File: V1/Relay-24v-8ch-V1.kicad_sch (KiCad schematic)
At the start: 49 parts, among them J1 Conn_01x09, J3 OUT1, J3 OUT2, J3 OUT3, J3 OUT4, J3 OUT5, J3 OUT6, J3 OUT7, J3 OUT8, K1 G5PZ-1A

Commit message: Change connector 3D model
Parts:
- J1: footprint Tales:TerminalBlock_Dorabo_DB141V-2.54-09P_1x09_P2.54mm_Vertical -> Tales:TerminalBlock_DG141V-2.54-9P_1x09_P2.54mm_Vertical
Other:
- title: (none) -> 8x 24V Relay Module

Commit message: Update to silkscreen and board image.
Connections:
- net +24V: now also J1.9 (Pin_9); no longer J1.1 (Pin_1)
- net at D14.1 (K), D15.2 (A), K1.4: now also J1.2 (Pin_2); no longer J1.8 (Pin_8)
- net at D14.1 (K), D15.2 (A), K1.4: now also J1.6 (Pin_6); no longer J1.4 (Pin_4)
- net at D14.1 (K), D15.2 (A), K1.4: now also J1.8 (Pin_8); no longer J1.2 (Pin_2)
- net at D14.1 (K), D15.2 (A), K1.4: now also J1.3 (Pin_3); no longer J1.7 (Pin_7)
- net at D14.1 (K), D15.2 (A), K1.4: now also J1.4 (Pin_4); no longer J1.6 (Pin_6)
- net at D14.1 (K), D15.2 (A), K1.4: now also J1.1 (Pin_1); no longer J1.9 (Pin_9)
- net at D14.1 (K), D15.2 (A), K1.4: now also J1.7 (Pin_7); no longer J1.3 (Pin_3)
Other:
- moved on the sheet: J1
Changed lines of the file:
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@@
     )
   )
-  (symbol (lib_id "Connector_Generic:Conn_01x09") (at 25.4 54.61 0) (mirror y) (unit 1)
-    (in_bom yes) (on_board yes) (dnp no) (fields_autoplaced)
-    (property "Reference" "J1" (at 25.4 39.37 0)
+  (symbol (lib_id "Connector_Generic:Conn_01x09") (at 25.4 54.61 180) (unit 1)
+    (in_bom yes) (on_board yes) (dnp no)
+    (property "Reference" "J1" (at 25.4 38.1 0)
       (effects (font (size 1.27 1.27)))
     )
-    (property "Value" "Conn_01x09" (at 25.4 41.91 0)
+    (property "Value" "Conn_01x09" (at 25.4 40.64 0)
       (effects (font (size 1.27 1.27)))
     )

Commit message: Adjustments for fabrication
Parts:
- D14: value BLUE/0603 -> GREEN/0603; LCSC Part # C72041 -> C72043; Mfr PN 19-217/BHC-ZL1M2RY/3T -> 19-217/GHC-YR1S2/3T; Vendor PN C72041 -> C72043
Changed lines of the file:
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@@
       (effects (font (size 1.27 1.27)) (justify left))
     )
-    (property "Value" "BLUE/0603" (at 68.58 153.67 90)
+    (property "Value" "GREEN/0603" (at 68.58 153.67 90)
       (effects (font (size 1.27 1.27)) (justify left))
     )
@@
       (effects (font (size 1.27 1.27)) hide)
     )
-    (property "Mfr PN" "19-217/BHC-ZL1M2RY/3T" (at 71.12 153.67 0)
+    (property "Mfr PN" "19-217/GHC-YR1S2/3T" (at 71.12 153.67 0)
       (effects (font (size 1.27 1.27)) hide)
     )
@@
       (effects (font (size 1.27 1.27)) hide)
     )
-    (property "Vendor PN" "C72041" (at 71.12 153.67 0)
-      (effects (font (size 1.27 1.27)) hide)
-    )
-    (property "LCSC Part #" "C72041" (at 68.58 156.21 90)
+    (property "Vendor PN" "C72043" (at 71.12 153.67 0)
+      (effects (font (size 1.27 1.27)) hide)
+    )
+    (property "LCSC Part #" "C72043" (at 68.58 156.21 90)
       (effects (font (size 1.27 1.27)) (justify left))
     )
@@
       (effects (font (size 1.27 1.27)) (justify left))
     )
-    (property "Value" "BLUE/0603" (at 171.45 78.74 90)
+    (property "Value" "GREEN/0603" (at 171.45 78.74 90)
       (effects (font (size 1.27 1.27)) (justify left))
     )
@@
       (effects (font (size 1.27 1.27)) hide)
     )
-    (property "Mfr PN" "19-217/BHC-ZL1M2RY/3T" (at 173.99 78.74 0)
+    (property "Mfr PN" "19-217/GHC-YR1S2/3T" (at 173.99 78.74 0)
       (effects (font (size 1.27 1.27)) hide)
     )
@@
       (effects (font (size 1.27 1.27)) hide)
     )
-    (property "Vendor PN" "C72041" (at 173.99 78.74 0)
-      (effects (font (size 1.27 1.27)) hide)
-    )
-    (property "LCSC Part #" "C72041" (at 171.45 81.28 90)
+    (property "Vendor PN" "C72043" (at 173.99 78.74 0)
+      (effects (font (size 1.27 1.27)) hide)
+    )
+    (property "LCSC Part #" "C72043" (at 171.45 81.28 90)
       (effects (font (size 1.27 1.27)) (justify left))
     )
@@
       (effects (font (size 1.27 1.27)) (justify left))
     )
-    (property "Value" "BLUE/0603" (at 68.58 116.84 90)
+    (property "Value" "GREEN/0603" (at 68.58 116.84 90)
       (effects (font (size 1.27 1.27)) (justify left))
     )
@@
       (effects (font (size 1.27 1.27)) hide)
     )
-    (property "Mfr PN" "19-217/BHC-ZL1M2RY/3T" (at 71.12 116.84 0)
+    (property "Mfr PN" "19-217/GHC-YR1S2/3T" (at 71.12 116.84 0)
       (effects (font (size 1.27 1.27)) hide)
     )
@@
       (effects (font (size 1.27 1.27)) hide)
     )
-    (property "Vendor PN" "C72041" (at 71.12 116.84 0)
-      (effects (font (size 1.27 1.27)) hide)
-    )
-    (property "LCSC Part #" "C72041" (at 68.58 119.38 90)
+    (property "Vendor PN" "C72043" (at 71.12 116.84 0)
+      (effects (font (size 1.27 1.27)) hide)
+    )
+    (property "LCSC Part #" "C72043" (at 68.58 119.38 90)
       (effects (font (size 1.27 1.27)) (justify left))
     )
@@
       (effects (font (size 1.27 1.27)) (justify left))
     )
-    (property "Value" "BLUE/0603" (at 68.58 78.74 90)
+    (property "Value" "GREEN/0603" (at 68.58 78.74 90)
       (effects (font (size 1.27 1.27)) (justify left))
     )
@@
       (effects (font (size 1.27 1.27)) hide)
     )
-    (property "Mfr PN" "19-217/BHC-ZL1M2RY/3T" (at 71.12 78.74 0)
+    (property "Mfr PN" "19-217/GHC-YR1S2/3T" (at 71.12 78.74 0)
       (effects (font (size 1.27 1.27)) hide)
     )
@@
       (effects (font (size 1.27 1.27)) hide)
     )
-    (property "Vendor PN" "C72041" (at 71.12 78.74 0)
-      (effects (font (size 1.27 1.27)) hide)
-    )
-    (property "LCSC Part #" "C72041" (at 68.58 81.28 90)
+    (property "Vendor PN" "C72043" (at 71.12 78.74 0)
+      (effects (font (size 1.27 1.27)) hide)
+    )
+    (property "LCSC Part #" "C72043" (at 68.58 81.28 90)
       (effects (font (size 1.27 1.27)) (justify left))
     )
@@
       (effects (font (size 1.27 1.27)) (justify left))
     )
-    (property "Value" "BLUE/0603" (at 171.45 153.67 90)
+    (property "Value" "GREEN/0603" (at 171.45 153.67 90)
       (effects (font (size 1.27 1.27)) (justify left))
     )
@@
       (effects (font (size 1.27 1.27)) hide)
     )
-    (property "Mfr PN" "19-217/BHC-ZL1M2RY/3T" (at 173.99 153.67 0)
+    (property "Mfr PN" "19-217/GHC-YR1S2/3T" (at 173.99 153.67 0)
       (effects (font (size 1.27 1.27)) hide)
     )
@@
       (effects (font (size 1.27 1.27)) hide)
     )
-    (property "Vendor PN" "C72041" (at 173.99 153.67 0)
-      (effects (font (size 1.27 1.27)) hide)
-    )
-    (property "LCSC Part #" "C72041" (at 171.45 156.21 90)
+    (property "Vendor PN" "C72043" (at 173.99 153.67 0)
+      (effects (font (size 1.27 1.27)) hide)
+    )
+    (property "LCSC Part #" "C72043" (at 171.45 156.21 90)
       (effects (font (size 1.27 1.27)) (justify left))
     )
@@
       (effects (font (size 1.27 1.27)) (justify left))
     )
-    (property "Value" "BLUE/0603" (at 68.58 40.64 90)
+    (property "Value" "GREEN/0603" (at 68.58 40.64 90)
       (effects (font (size 1.27 1.27)) (justify left))
     )
@@
       (effects (font (size 1.27 1.27)) hide)
     )
-    (property "Mfr PN" "19-217/BHC-ZL1M2RY/3T" (at 71.12 40.64 0)
+    (property "Mfr PN" "19-217/GHC-YR1S2/3T" (at 71.12 40.64 0)
       (effects (font (size 1.27 1.27)) hide)
     )
@@
       (effects (font (size 1.27 1.27)) hide)
     )
-    (property "Vendor PN" "C72041" (at 71.12 40.64 0)
-      (effects (font (size 1.27 1.27)) hide)
-    )
-    (property "LCSC Part #" "C72041" (at 68.58 43.18 90)
+    (property "Vendor PN" "C72043" (at 71.12 40.64 0)
+      (effects (font (size 1.27 1.27)) hide)
+    )
+    (property "LCSC Part #" "C72043" (at 68.58 43.18 90)
       (effects (font (size 1.27 1.27)) (justify left))
     )
@@
       (effects (font (size 1.27 1.27)) (justify left))
     )
-    (property "Value" "BLUE/0603" (at 171.45 116.84 90)
+    (property "Value" "GREEN/0603" (at 171.45 116.84 90)
       (effects (font (size 1.27 1.27)) (justify left))
     )
@@
       (effects (font (size 1.27 1.27)) hide)
     )
-    (property "Mfr PN" "19-217/BHC-ZL1M2RY/3T" (at 173.99 116.84 0)
+    (property "Mfr PN" "19-217/GHC-YR1S2/3T" (at 173.99 116.84 0)
       (effects (font (size 1.27 1.27)) hide)
     )
@@
       (effects (font (size 1.27 1.27)) hide)
     )
-    (property "Vendor PN" "C72041" (at 173.99 116.84 0)
-      (effects (font (size 1.27 1.27)) hide)
-    )
-    (property "LCSC Part #" "C72041" (at 171.45 119.38 90)
+    (property "Vendor PN" "C72043" (at 173.99 116.84 0)
+      (effects (font (size 1.27 1.27)) hide)
+    )
+    (property "LCSC Part #" "C72043" (at 171.45 119.38 90)
       (effects (font (size 1.27 1.27)) (justify left))
     )
@@
       (effects (font (size 1.27 1.27)) (justify left))
     )
-    (property "Value" "BLUE/0603" (at 171.45 40.64 90)
+    (property "Value" "GREEN/0603" (at 171.45 40.64 90)
       (effects (font (size 1.27 1.27)) (justify left))
     )
@@
       (effects (font (size 1.27 1.27)) hide)
     )
-    (property "Mfr PN" "19-217/BHC-ZL1M2RY/3T" (at 173.99 40.64 0)
+    (property "Mfr PN" "19-217/GHC-YR1S2/3T" (at 173.99 40.64 0)
       (effects (font (size 1.27 1.27)) hide)
     )
@@
       (effects (font (size 1.27 1.27)) hide)
     )
-    (property "Vendor PN" "C72041" (at 173.99 40.64 0)
-      (effects (font (size 1.27 1.27)) hide)
-    )
-    (property "LCSC Part #" "C72041" (at 171.45 43.18 90)
-      (effects (font (size 1.27 1.27)) (justify left))
-    )
+    (property "Vendor PN" "C72043" (at 173.99 40.64 0)
+      (effects (font (size 1.27 1.27)) hide)
+    )
+    (property "LCSC Part #" "C72043" (at 171.45 43.18 90)
+      (effects (font (size 1.27 1.27)) (justify left))
+    )

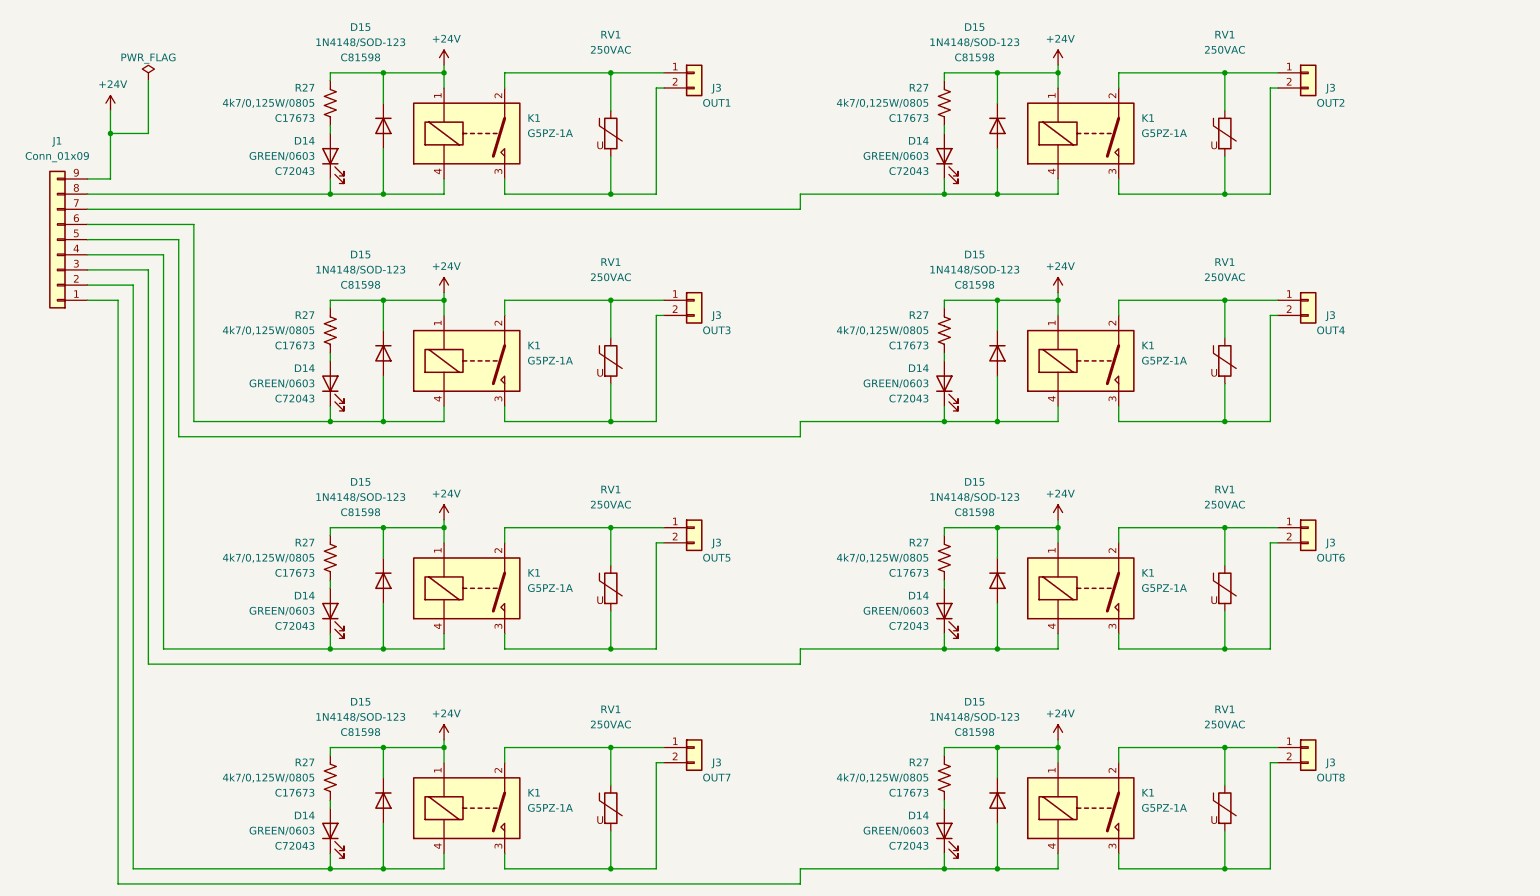
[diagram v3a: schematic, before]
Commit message: Varistor updated
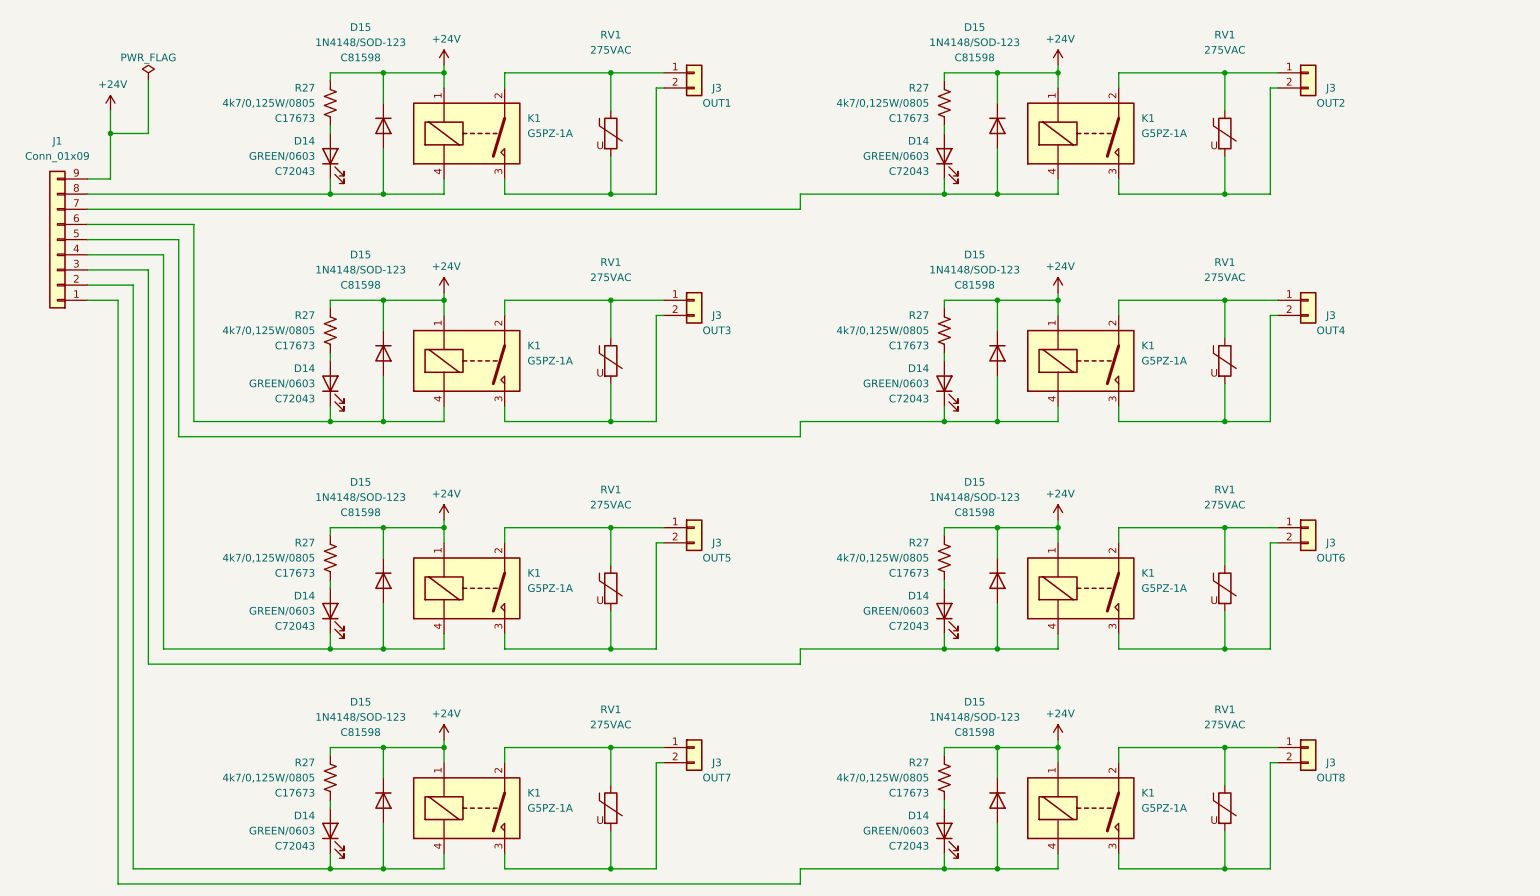
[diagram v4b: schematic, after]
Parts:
- RV1: value 250VAC -> 275VAC; Mfr PN 391KD10 -> 431KD10; Vendor PN 603-391KD10 -> 603-431KD10
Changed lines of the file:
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@@
       (effects (font (size 1.27 1.27)))
     )
-    (property "Value" "250VAC" (at 118.11 99.06 0)
+    (property "Value" "275VAC" (at 118.11 99.06 0)
       (effects (font (size 1.27 1.27)))
     )
@@
       (effects (font (size 1.27 1.27)) hide)
     )
-    (property "Mfr PN" "391KD10" (at 118.11 113.03 0)
+    (property "Mfr PN" "431KD10" (at 118.11 113.03 0)
       (effects (font (size 1.27 1.27)) hide)
     )
@@
       (effects (font (size 1.27 1.27)) hide)
     )
-    (property "Vendor PN" "603-391KD10" (at 118.11 113.03 0)
+    (property "Vendor PN" "603-431KD10" (at 118.11 113.03 0)
       (effects (font (size 1.27 1.27)) hide)
     )
@@
       (effects (font (size 1.27 1.27)))
     )
-    (property "Value" "250VAC" (at 220.98 135.89 0)
+    (property "Value" "275VAC" (at 220.98 135.89 0)
       (effects (font (size 1.27 1.27)))
     )
@@
       (effects (font (size 1.27 1.27)) hide)
     )
-    (property "Mfr PN" "391KD10" (at 220.98 149.86 0)
+    (property "Mfr PN" "431KD10" (at 220.98 149.86 0)
       (effects (font (size 1.27 1.27)) hide)
     )
@@
       (effects (font (size 1.27 1.27)) hide)
     )
-    (property "Vendor PN" "603-391KD10" (at 220.98 149.86 0)
+    (property "Vendor PN" "603-431KD10" (at 220.98 149.86 0)
       (effects (font (size 1.27 1.27)) hide)
     )
@@
       (effects (font (size 1.27 1.27)))
     )
-    (property "Value" "250VAC" (at 220.98 60.96 0)
+    (property "Value" "275VAC" (at 220.98 60.96 0)
       (effects (font (size 1.27 1.27)))
     )
@@
       (effects (font (size 1.27 1.27)) hide)
     )
-    (property "Mfr PN" "391KD10" (at 220.98 74.93 0)
+    (property "Mfr PN" "431KD10" (at 220.98 74.93 0)
       (effects (font (size 1.27 1.27)) hide)
     )
@@
       (effects (font (size 1.27 1.27)) hide)
     )
-    (property "Vendor PN" "603-391KD10" (at 220.98 74.93 0)
+    (property "Vendor PN" "603-431KD10" (at 220.98 74.93 0)
       (effects (font (size 1.27 1.27)) hide)
     )
@@
       (effects (font (size 1.27 1.27)))
     )
-    (property "Value" "250VAC" (at 220.98 22.86 0)
+    (property "Value" "275VAC" (at 220.98 22.86 0)
       (effects (font (size 1.27 1.27)))
     )
@@
       (effects (font (size 1.27 1.27)) hide)
     )
-    (property "Mfr PN" "391KD10" (at 220.98 36.83 0)
+    (property "Mfr PN" "431KD10" (at 220.98 36.83 0)
       (effects (font (size 1.27 1.27)) hide)
     )
@@
       (effects (font (size 1.27 1.27)) hide)
     )
-    (property "Vendor PN" "603-391KD10" (at 220.98 36.83 0)
+    (property "Vendor PN" "603-431KD10" (at 220.98 36.83 0)
       (effects (font (size 1.27 1.27)) hide)
     )
@@
       (effects (font (size 1.27 1.27)))
     )
-    (property "Value" "250VAC" (at 118.11 135.89 0)
+    (property "Value" "275VAC" (at 118.11 135.89 0)
       (effects (font (size 1.27 1.27)))
     )
@@
       (effects (font (size 1.27 1.27)) hide)
     )
-    (property "Mfr PN" "391KD10" (at 118.11 149.86 0)
+    (property "Mfr PN" "431KD10" (at 118.11 149.86 0)
       (effects (font (size 1.27 1.27)) hide)
     )
@@
       (effects (font (size 1.27 1.27)) hide)
     )
-    (property "Vendor PN" "603-391KD10" (at 118.11 149.86 0)
+    (property "Vendor PN" "603-431KD10" (at 118.11 149.86 0)
       (effects (font (size 1.27 1.27)) hide)
     )
@@
       (effects (font (size 1.27 1.27)))
     )
-    (property "Value" "250VAC" (at 220.98 99.06 0)
+    (property "Value" "275VAC" (at 220.98 99.06 0)
       (effects (font (size 1.27 1.27)))
     )
@@
       (effects (font (size 1.27 1.27)) hide)
     )
-    (property "Mfr PN" "391KD10" (at 220.98 113.03 0)
+    (property "Mfr PN" "431KD10" (at 220.98 113.03 0)
       (effects (font (size 1.27 1.27)) hide)
     )
@@
       (effects (font (size 1.27 1.27)) hide)
     )
-    (property "Vendor PN" "603-391KD10" (at 220.98 113.03 0)
+    (property "Vendor PN" "603-431KD10" (at 220.98 113.03 0)
       (effects (font (size 1.27 1.27)) hide)
     )
@@
       (effects (font (size 1.27 1.27)))
     )
-    (property "Value" "250VAC" (at 118.11 22.86 0)
+    (property "Value" "275VAC" (at 118.11 22.86 0)
       (effects (font (size 1.27 1.27)))
     )
@@
       (effects (font (size 1.27 1.27)) hide)
     )
-    (property "Mfr PN" "391KD10" (at 118.11 36.83 0)
+    (property "Mfr PN" "431KD10" (at 118.11 36.83 0)
       (effects (font (size 1.27 1.27)) hide)
     )
@@
       (effects (font (size 1.27 1.27)) hide)
     )
-    (property "Vendor PN" "603-391KD10" (at 118.11 36.83 0)
+    (property "Vendor PN" "603-431KD10" (at 118.11 36.83 0)
       (effects (font (size 1.27 1.27)) hide)
     )
@@
       (effects (font (size 1.27 1.27)))
     )
-    (property "Value" "250VAC" (at 118.11 60.96 0)
+    (property "Value" "275VAC" (at 118.11 60.96 0)
       (effects (font (size 1.27 1.27)))
     )
@@
       (effects (font (size 1.27 1.27)) hide)
     )
-    (property "Mfr PN" "391KD10" (at 118.11 74.93 0)
+    (property "Mfr PN" "431KD10" (at 118.11 74.93 0)
       (effects (font (size 1.27 1.27)) hide)
     )
@@
       (effects (font (size 1.27 1.27)) hide)
     )
-    (property "Vendor PN" "603-391KD10" (at 118.11 74.93 0)
-      (effects (font (size 1.27 1.27)) hide)
-    )
+    (property "Vendor PN" "603-431KD10" (at 118.11 74.93 0)
+      (effects (font (size 1.27 1.27)) hide)
+    )
